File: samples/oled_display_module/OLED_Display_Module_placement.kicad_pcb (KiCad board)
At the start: 2 copper layers, 71 x 70 mm, 4 parts, among them J1 USB-C, U1 TLV75518, U2 SSD1306, U3 TXS0102

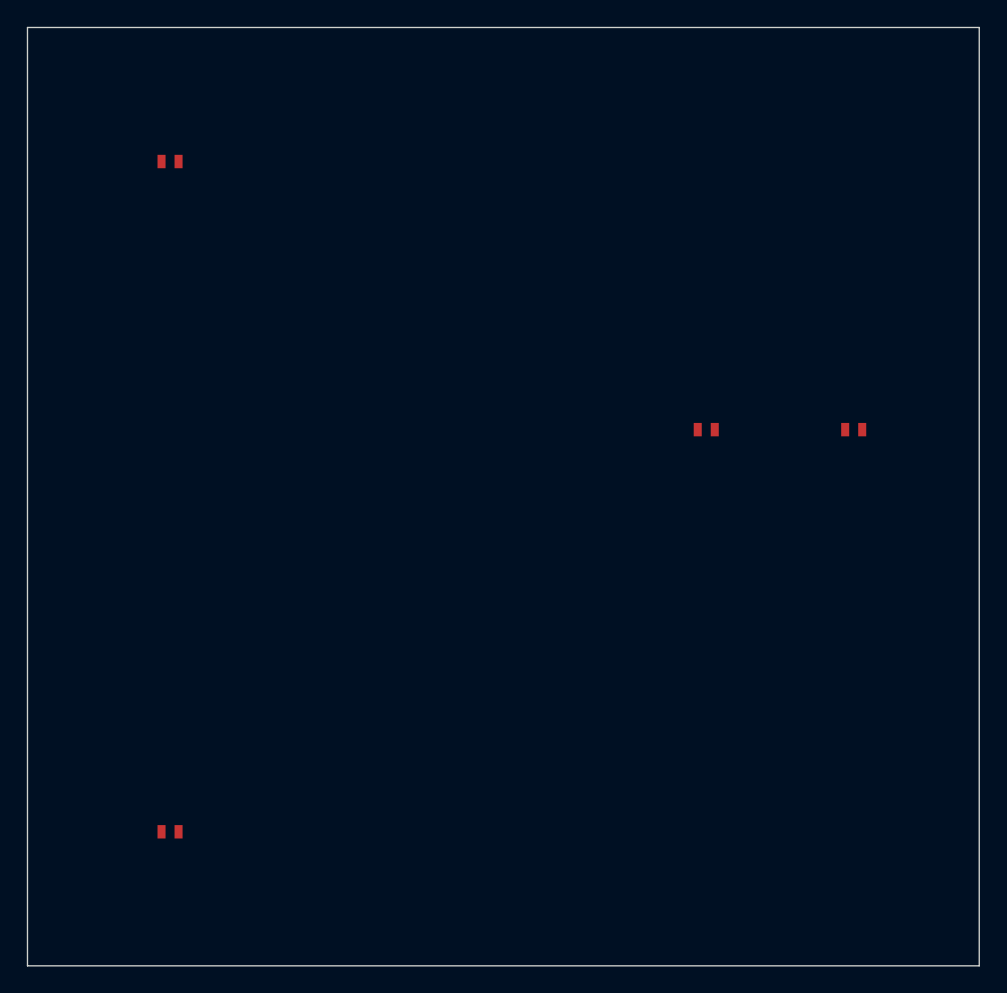
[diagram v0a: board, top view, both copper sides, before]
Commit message: chore: regenerate 8 sample designs against v0.27.0 engine
All 8 samples pass full validation (0 ERC errors):
- led_power_indicator, iot_sensor_node, usb_regulated_supply,
  usb_uart_bridge, oled_display_module, battery_iot_sensor,
  motor_controller, fpga_power_carrier

New artifacts per sample: .kicad_sch, _test_points.csv, _pinout.csv,
canonical_spec.yaml, design_ir.json, validation_report.json; MCU samples
also emit sdkconfig.defaults / .ioc stubs.

Also adds samples/*/svg/ to .gitignore — schematic SVG exports are
regenerable and too large to track.

zigbee_humidistat deferred: non-deterministic schematic output across
two generation runs (text annotation ordering vs sheet_instances).
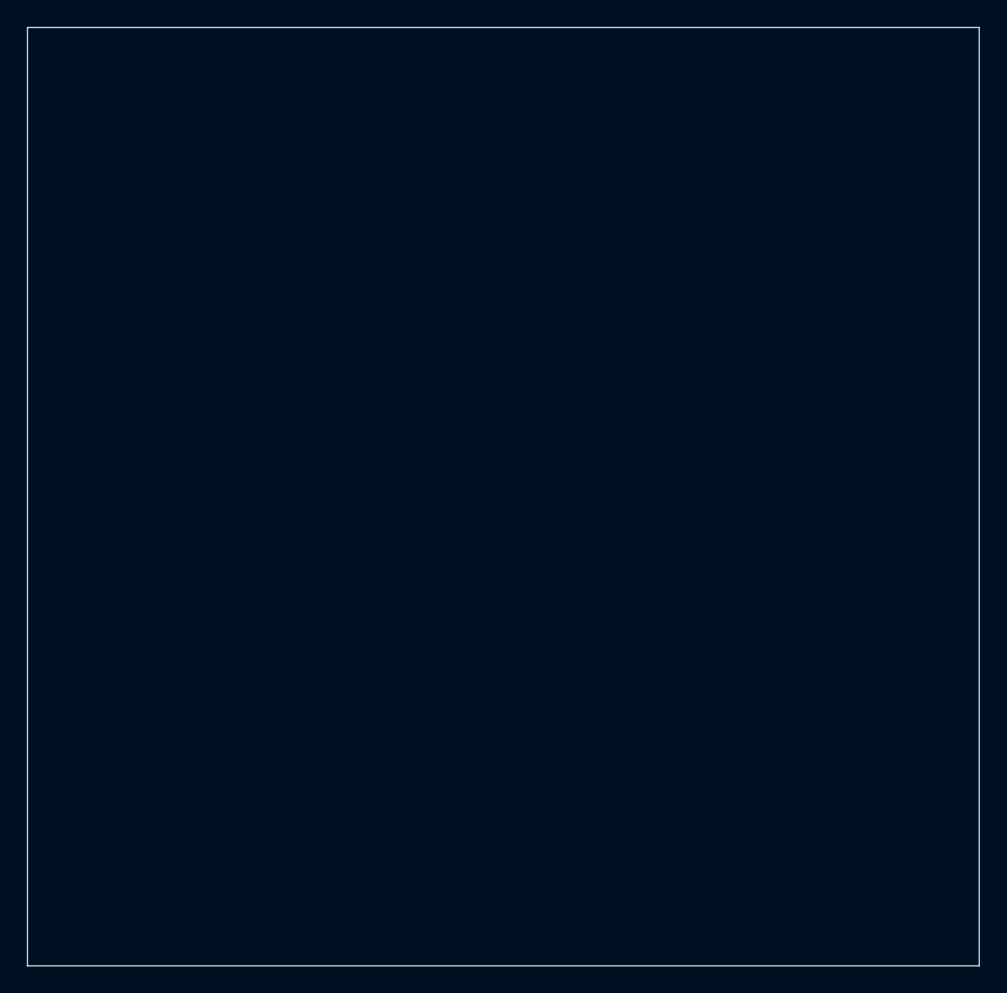
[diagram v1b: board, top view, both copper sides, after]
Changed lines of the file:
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@@
-(kicad_pcb (version 20240108) (generator "schematic_engine")
+(kicad_pcb (version 20240108) (generator "schematic_engine placement_preview")
   (general (thickness 1.6) (legacy_teardrops no))
   (layers
@@
       (effects (font (size 1.0 1.0) (thickness 0.15)))
     )
-    (pad "1" smd rect (at 0.00 0) (size 0.6 1.0) (layers "F.Cu" "F.Paste" "F.Mask") (net 15 "VBUS_5V"))
-    (pad "2" smd rect (at 1.27 0) (size 0.6 1.0) (layers "F.Cu" "F.Paste" "F.Mask") (net 3 "GND"))
   )
   (footprint "SSD1306_Module"
@@
       (effects (font (size 1.0 1.0) (thickness 0.15)))
     )
-    (pad "1" smd rect (at 0.00 0) (size 0.6 1.0) (layers "F.Cu" "F.Paste" "F.Mask") (net 18 "VDD_3P3"))
-    (pad "2" smd rect (at 1.27 0) (size 0.6 1.0) (layers "F.Cu" "F.Paste" "F.Mask") (net 3 "GND"))
   )
   (footprint "Package_TO_SOT_SMD:SOT-23-8"
@@
       (effects (font (size 1.0 1.0) (thickness 0.15)))
     )
-    (pad "1" smd rect (at 0.00 0) (size 0.6 1.0) (layers "F.Cu" "F.Paste" "F.Mask") (net 17 "VDD_1P8"))
-    (pad "2" smd rect (at 1.27 0) (size 0.6 1.0) (layers "F.Cu" "F.Paste" "F.Mask") (net 18 "VDD_3P3"))
   )
   (footprint "Connector_USB:USB_C_Receptacle_GCT_USB4085"
@@
       (effects (font (size 1.0 1.0) (thickness 0.15)))
     )
-    (pad "1" smd rect (at 0.00 0) (size 0.6 1.0) (layers "F.Cu" "F.Paste" "F.Mask") (net 15 "VBUS_5V"))
-    (pad "2" smd rect (at 1.27 0) (size 0.6 1.0) (layers "F.Cu" "F.Paste" "F.Mask") (net 3 "GND"))
   )
   (gr_line (start 0.00 0.00) (end 71.00 0.00) (stroke (width 0.1) (type solid)) (layer "Edge.Cuts"))
